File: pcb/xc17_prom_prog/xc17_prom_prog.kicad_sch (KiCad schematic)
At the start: 0 parts

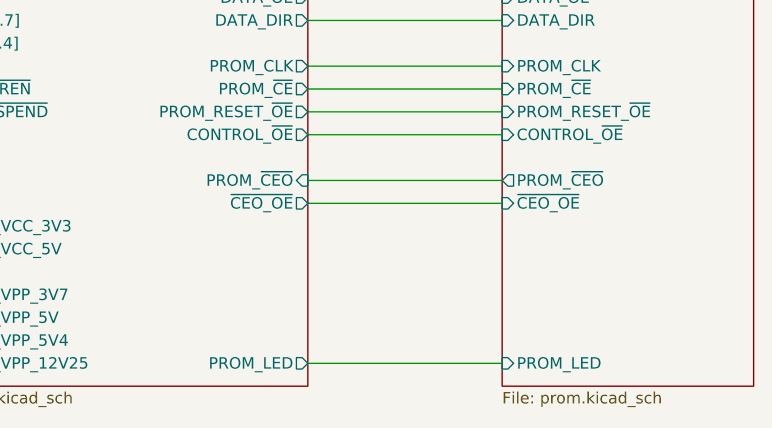
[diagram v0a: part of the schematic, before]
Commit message: Fix MOSFETs
 * Block MOSFET body diodes by placing two MOSFETs in anti series.
 * Connect PROM LED to pin header.
 * Add transistors to actively pull PROM VCC and VPP low.
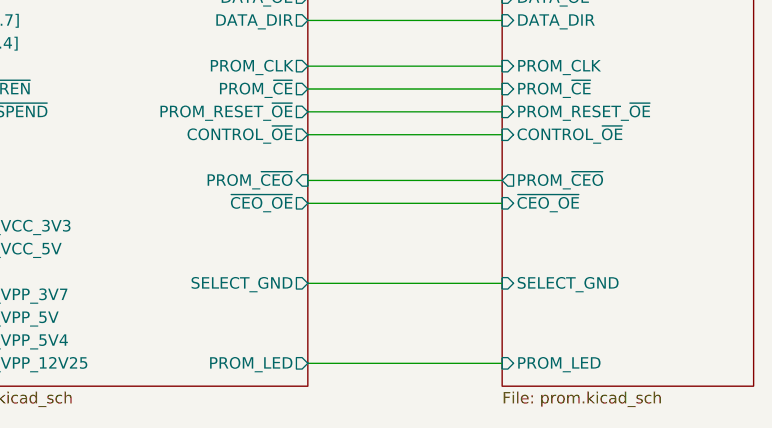
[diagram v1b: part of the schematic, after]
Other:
- sheet FPGA ports: added SELECT_GND; removed none
- sheet PROM ports: added SELECT_GND; removed none
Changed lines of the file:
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@@
 	(title_block
 		(title "XC17xxx PROM Programmer")
-		(date "2024-11-02")
-		(rev "0")
+		(date "2024-11-23")
+		(rev "1")
 		(company "CC-BY-SA-4.0 Michael Singer")
 		(comment 1 "https://github.com/msinger/xc17_prom_prog/")
@@
 		(pts
 			(xy 106.68 105.41) (xy 128.27 105.41)
+		)
+		(stroke
+			(width 0)
+			(type default)
+		)
+	)
+	(wire
+		(pts
+			(xy 171.45 109.22) (xy 193.04 109.22)
 		)
 		(stroke
@@
 			)
 		)
+		(pin "SELECT_GND" input
+			(at 193.04 109.22 180)
+			(effects
+				(font
+					(size 1.27 1.27)
+				)
+				(justify left)
+			)
+		)
 		(instances
 			(project "xc17_prom_prog"
@@
 			(effects
 				(font
+					(size 1.27 1.27)
+				)
+				(justify right)
+			)
+		)
+		(pin "SELECT_GND" output
+			(at 171.45 109.22 0)
+			(effects
+				(font

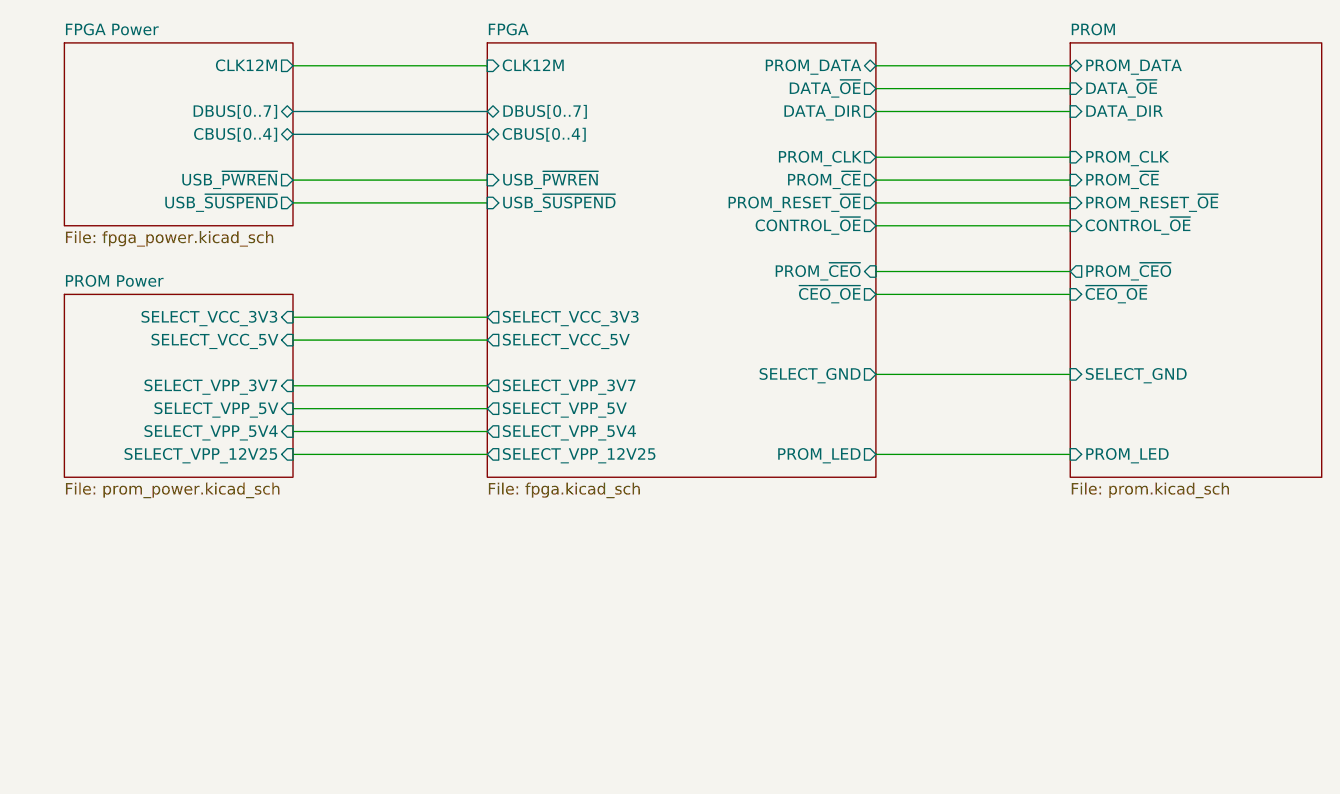
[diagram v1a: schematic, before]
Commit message: Implement more precise voltage controls
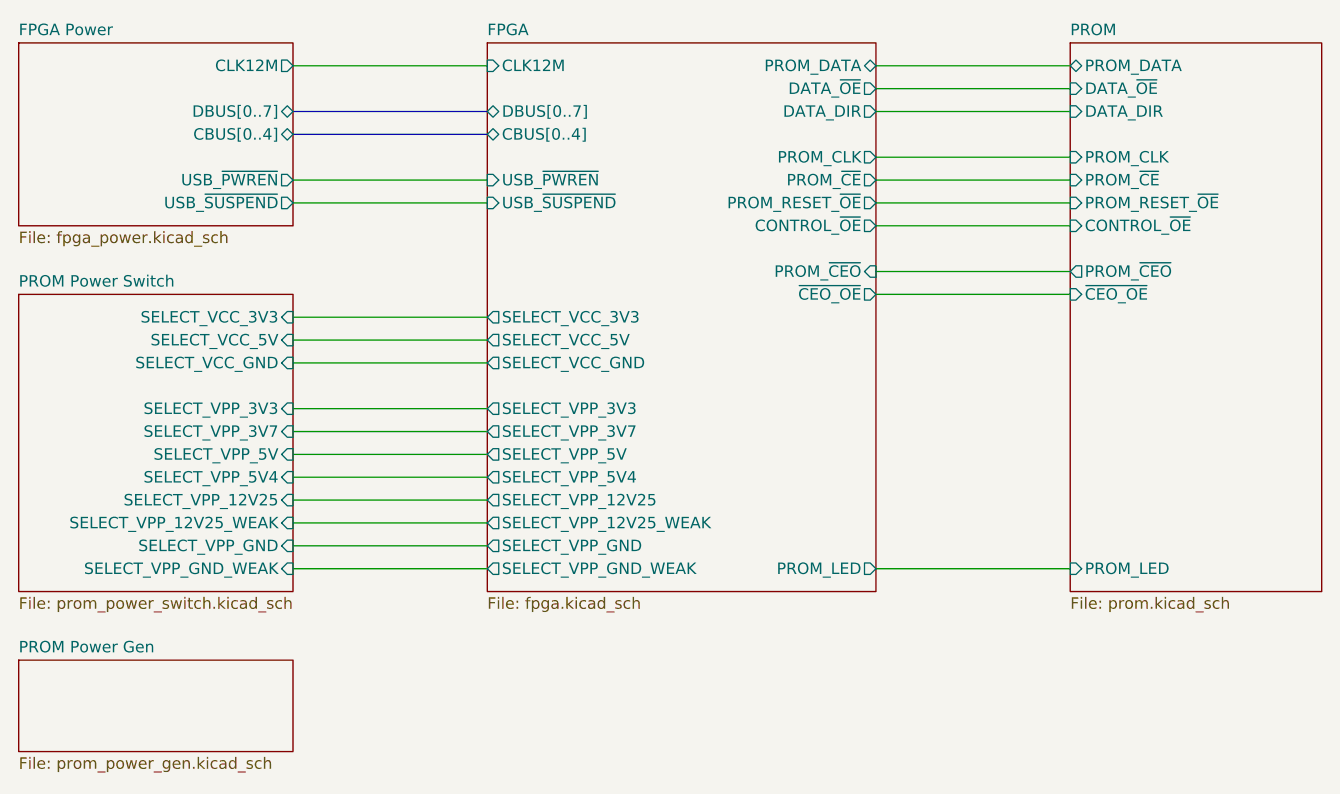
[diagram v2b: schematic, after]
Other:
- sheet PROM Power renamed PROM Power Switch
- added sheet PROM Power Gen (prom_power_gen.kicad_sch)
- sheet FPGA ports: added SELECT_VCC_GND, SELECT_VPP_12V25_WEAK, SELECT_VPP_3V3, SELECT_VPP_GND, SELECT_VPP_GND_WEAK; removed SELECT_GND
- sheet PROM ports: added none; removed SELECT_GND
- sheet PROM Power Switch: file prom_power.kicad_sch -> prom_power_switch.kicad_sch
- sheet PROM Power Switch ports: added SELECT_VCC_GND, SELECT_VPP_12V25_WEAK, SELECT_VPP_3V3, SELECT_VPP_GND, SELECT_VPP_GND_WEAK; removed none

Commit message: Remove unused components
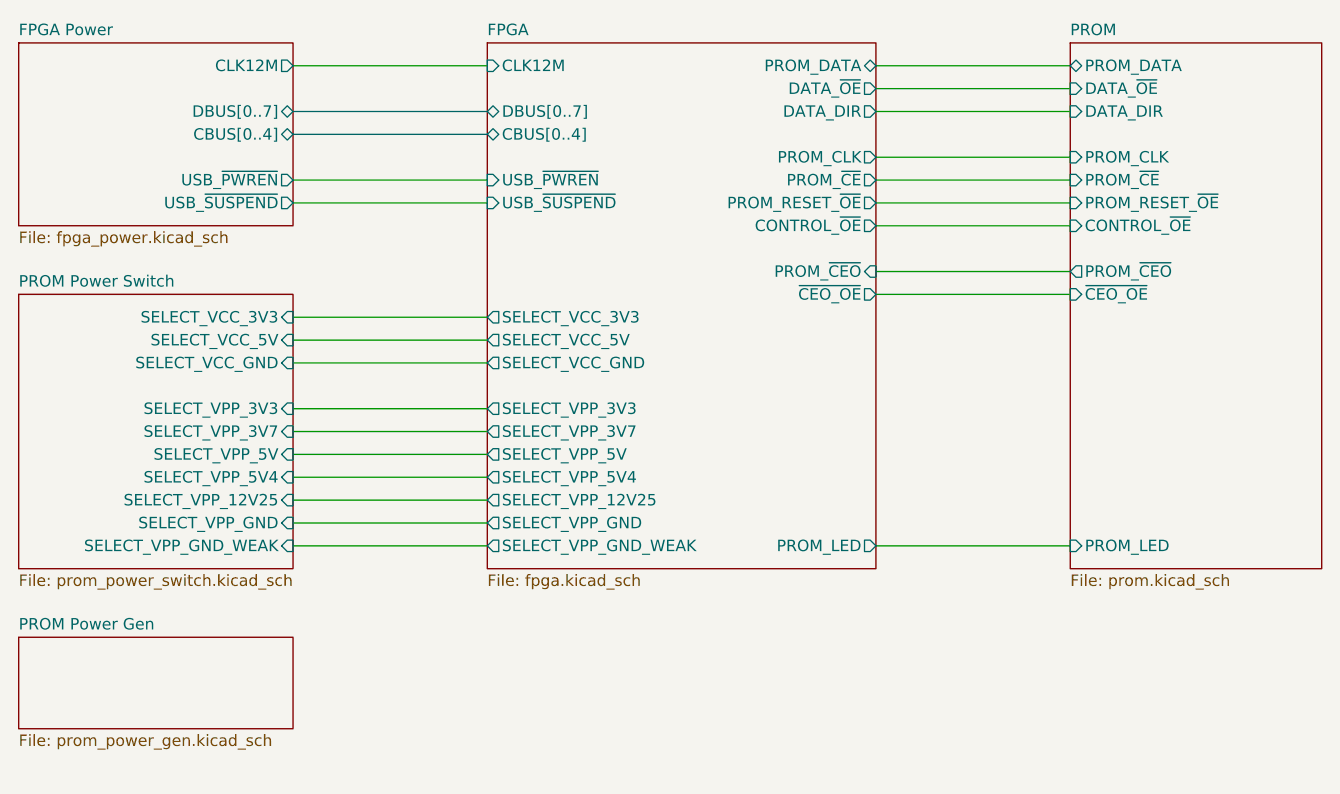
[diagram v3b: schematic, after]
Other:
- sheet FPGA ports: added none; removed SELECT_VPP_12V25_WEAK
- sheet PROM Power Switch ports: added none; removed SELECT_VPP_12V25_WEAK
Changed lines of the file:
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@@
 	(title_block
 		(title "XC17xxx PROM Programmer")
-		(date "2024-12-08")
-		(rev "2")
+		(date "2025-01-29")
+		(rev "3")
 		(company "CC-BY-SA-4.0 Michael Singer")
 		(comment 1 "https://github.com/msinger/xc17_prom_prog/")
@@
 	(wire
 		(pts
-			(xy 106.68 130.81) (xy 128.27 130.81)
+			(xy 106.68 128.27) (xy 128.27 128.27)
 		)
 		(stroke
@@
 	(wire
 		(pts
+			(xy 171.45 85.09) (xy 193.04 85.09)
+		)
+		(stroke
+			(width 0)
+			(type default)
+		)
+	)
+	(wire
+		(pts
+			(xy 106.68 74.93) (xy 128.27 74.93)
+		)
+		(stroke
+			(width 0)
+			(type default)
+		)
+	)
+	(wire
+		(pts
+			(xy 171.45 97.79) (xy 193.04 97.79)
+		)
+		(stroke
+			(width 0)
+			(type default)
+		)
+	)
+	(wire
+		(pts
+			(xy 106.68 115.57) (xy 128.27 115.57)
+		)
+		(stroke
+			(width 0)
+			(type default)
+		)
+	)
+	(wire
+		(pts
+			(xy 106.68 105.41) (xy 128.27 105.41)
+		)
+		(stroke
+			(width 0)
+			(type default)
+		)
+	)
+	(wire
+		(pts
 			(xy 106.68 125.73) (xy 128.27 125.73)
 		)
@@
 	(wire
 		(pts
-			(xy 171.45 130.81) (xy 193.04 130.81)
-		)
-		(stroke
-			(width 0)
-			(type default)
-		)
-	)
-	(wire
-		(pts
-			(xy 171.45 85.09) (xy 193.04 85.09)
-		)
-		(stroke
-			(width 0)
-			(type default)
-		)
-	)
-	(wire
-		(pts
-			(xy 106.68 74.93) (xy 128.27 74.93)
-		)
-		(stroke
-			(width 0)
-			(type default)
-		)
-	)
-	(wire
-		(pts
-			(xy 171.45 97.79) (xy 193.04 97.79)
-		)
-		(stroke
-			(width 0)
-			(type default)
-		)
-	)
-	(wire
-		(pts
-			(xy 106.68 115.57) (xy 128.27 115.57)
-		)
-		(stroke
-			(width 0)
-			(type default)
-		)
-	)
-	(wire
-		(pts
-			(xy 106.68 105.41) (xy 128.27 105.41)
-		)
-		(stroke
-			(width 0)
-			(type default)
-		)
-	)
-	(wire
-		(pts
-			(xy 106.68 128.27) (xy 128.27 128.27)
-		)
-		(stroke
-			(width 0)
-			(type default)
-		)
-	)
-	(wire
-		(pts
 			(xy 106.68 120.65) (xy 128.27 120.65)
 		)
@@
 		(pts
 			(xy 106.68 80.01) (xy 128.27 80.01)
+		)
+		(stroke
+			(width 0)
+			(type default)
+		)
+	)
+	(wire
+		(pts
+			(xy 171.45 128.27) (xy 193.04 128.27)
 		)
 		(stroke
@@
 	(sheet
 		(at 193.04 72.39)
-		(size 27.94 60.96)
+		(size 27.94 58.42)
 		(fields_autoplaced yes)
 		(stroke
@@
 		)
 		(property "Sheetfile" "prom.kicad_sch"
-			(at 193.04 133.9346 0)
+			(at 193.04 131.3946 0)
 			(effects
 				(font
@@
 		)
 		(pin "PROM_LED" input
-			(at 193.04 130.81 180)
+			(at 193.04 128.27 180)
 			(effects
 				(font
@@
 	(sheet
 		(at 76.2 100.33)
-		(size 30.48 33.02)
+		(size 30.48 30.48)
 		(fields_autoplaced yes)
 		(stroke
@@
 		)
 		(property "Sheetfile" "prom_power_switch.kicad_sch"
-			(at 76.2 133.9346 0)
+			(at 76.2 131.3946 0)
 			(effects
 				(font
@@
 		)
 		(pin "SELECT_VPP_GND" input
+			(at 106.68 125.73 0)
+			(effects
+				(font
+					(size 1.27 1.27)
+				)
+				(justify right)
+			)
+		)
+		(pin "SELECT_VPP_GND_WEAK" input
 			(at 106.68 128.27 0)
-			(effects
-				(font
-					(size 1.27 1.27)
-				)
-				(justify right)
-			)
-		)
-		(pin "SELECT_VPP_GND_WEAK" input
-			(at 106.68 130.81 0)
-			(effects
-				(font
-					(size 1.27 1.27)
-				)
-				(justify right)
-			)
-		)
-		(pin "SELECT_VPP_12V25_WEAK" input
-			(at 106.68 125.73 0)
 			(effects
 				(font
@@
 	)
 	(sheet
-		(at 76.2 140.97)
+		(at 76.2 138.43)
 		(size 30.48 10.16)
 		(fields_autoplaced yes)
@@
 		)
 		(property "Sheetname" "PROM Power Gen"
-			(at 76.2 140.2584 0)
+			(at 76.2 137.7184 0)
 			(effects
 				(font
@@
 		)
 		(property "Sheetfile" "prom_power_gen.kicad_sch"
-			(at 76.2 151.7146 0)
+			(at 76.2 149.1746 0)
 			(effects
 				(font
@@
 	(sheet
 		(at 128.27 72.39)
-		(size 43.18 60.96)
+		(size 43.18 58.42)
 		(fields_autoplaced yes)
 		(stroke
@@
 		)
 		(property "Sheetfile" "fpga.kicad_sch"
-			(at 128.27 133.9346 0)
+			(at 128.27 131.3946 0)
 			(effects
 				(font
@@
 		)
 		(pin "PROM_LED" output
-			(at 171.45 130.81 0)
+			(at 171.45 128.27 0)
 			(effects
 				(font
@@
 		)
 		(pin "SELECT_VPP_GND" output
+			(at 128.27 125.73 180)
+			(effects
+				(font
+					(size 1.27 1.27)
+				)
+				(justify left)
+			)
+		)
+		(pin "SELECT_VPP_GND_WEAK" output
 			(at 128.27 128.27 180)
-			(effects
-				(font
-					(size 1.27 1.27)
-				)
-				(justify left)
-			)
-		)
-		(pin "SELECT_VPP_GND_WEAK" output
-			(at 128.27 130.81 180)
 			(effects
 				(font
@@
 			(effects
 				(font
-					(size 1.27 1.27)
-				)
-				(justify left)
-			)
-		)
-		(pin "SELECT_VPP_12V25_WEAK" output
-			(at 128.27 125.73 180)
-			(effects
-				(font
